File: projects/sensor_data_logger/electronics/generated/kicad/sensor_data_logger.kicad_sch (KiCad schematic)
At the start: 12 parts, among them J1 USB-C POWER, J2 UART DEBUG, U1 ESP32-S3-WROOM-1, U2 ICM-42688-P, U3 3V3 Buck

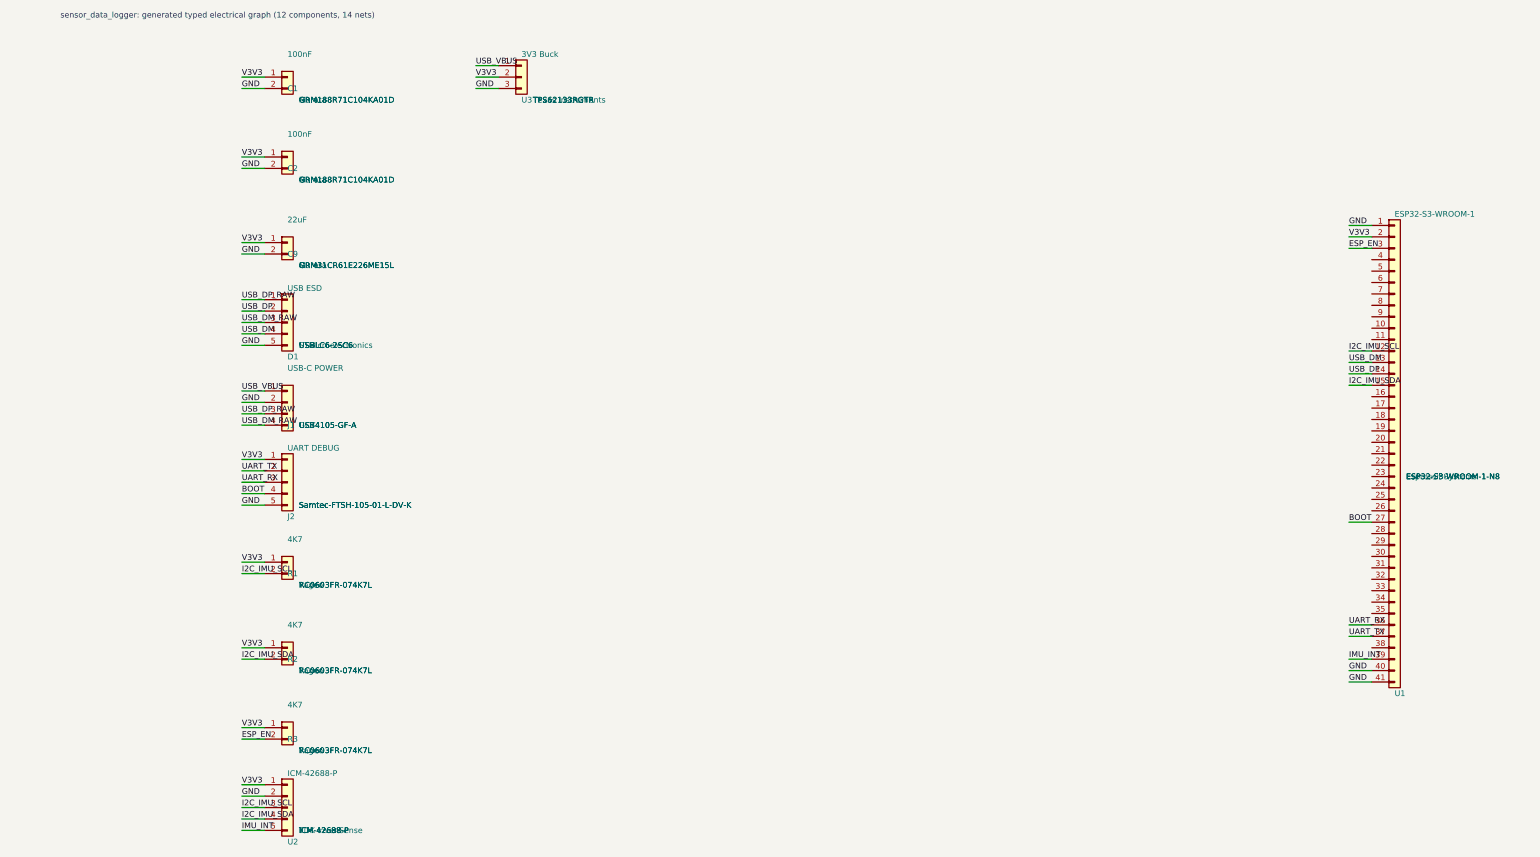
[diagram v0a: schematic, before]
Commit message: fix: sensor_data_logger autorouting pass; add BLE supplier records
- sensor_data_logger: freerouting run to completion, 0 unrouted (routing.json status=pass)
- parts/suppliers/curated.yaml: add nRF52840, BQ24079, BQ27441, JST PH 2-pin,
  SHT31 records for BLE sensor node to resolve supplier_record_missing failures
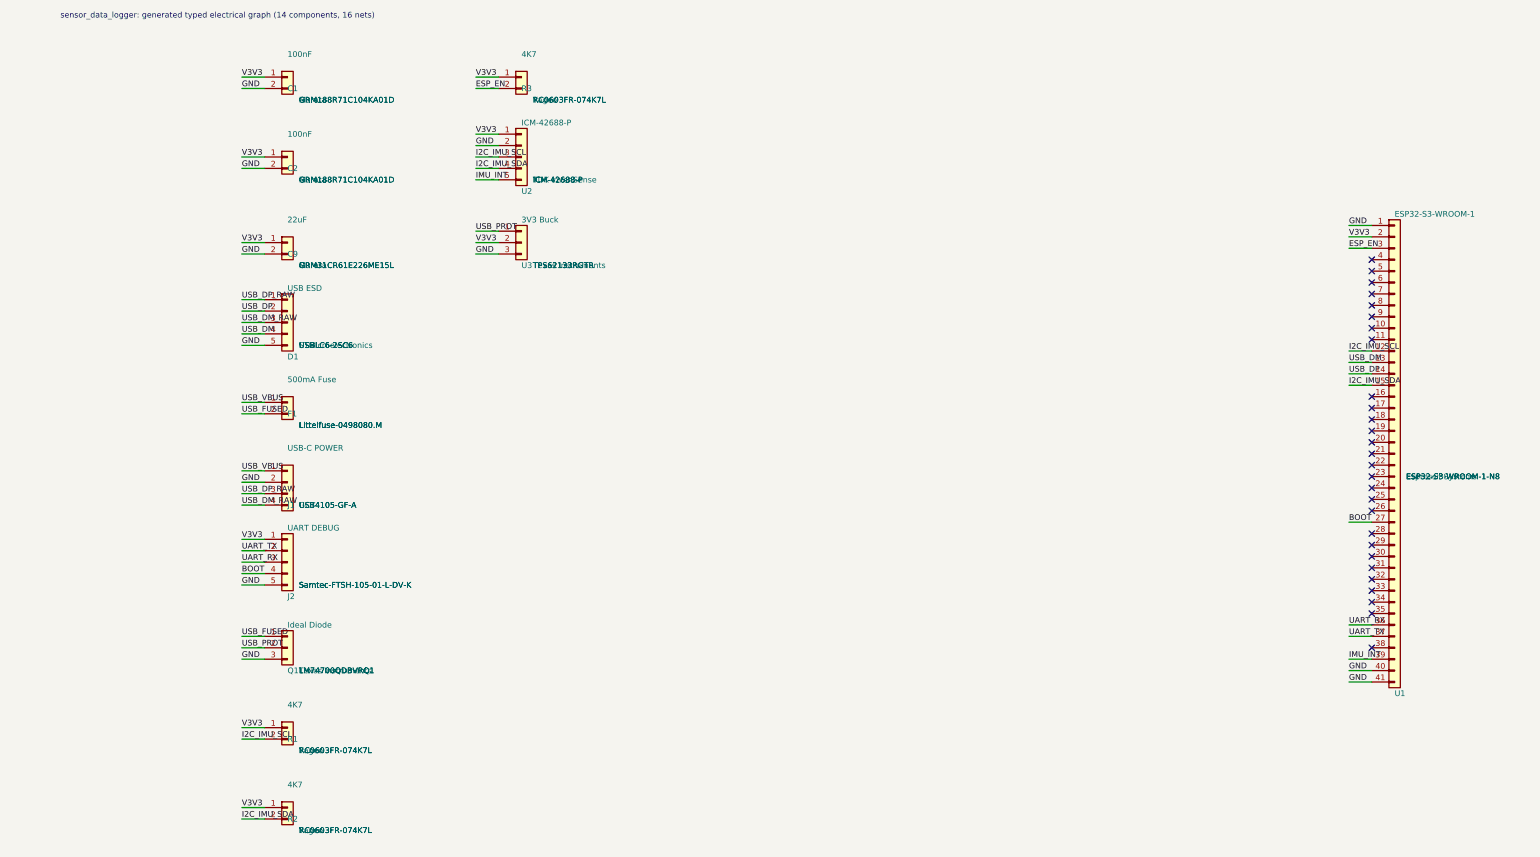
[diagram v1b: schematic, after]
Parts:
- added J1: USB-C POWER, USB_C_16Pin, symbol Connector_Generic:Conn_01x04
- added R2: 4K7, R0603, symbol Connector_Generic:Conn_01x02
- C1, C2: footprint Capacitor_SMD:C_0603_1608Metric -> C0603
- C9: footprint Capacitor_SMD:C_1206_3216Metric -> C1206
- D1: footprint Package_TO_SOT_SMD:SOT-23-6 -> SOT23-6
- F1: renamed from J1; value USB-C POWER -> 500mA Fuse; footprint Connector_USB:USB_C_GCT_USB4105 -> MIDI; symbol Connector_Generic:Conn_01x04 -> Connector_Generic:Conn_01x02; MPN USB4105-GF-A -> Littelfuse-0498080.M; Manufacturer GCT -> Littelfuse; Supplier_SKU USB4105-GF-A -> Littelfuse-0498080.M
- J2: footprint Connector_Samtec:FTSH-105 -> Cortex_Debug_10Pin
- Q1: renamed from R2; value 4K7 -> Ideal Diode; footprint Resistor_SMD:R_0603_1608Metric -> SOT23-6; symbol Connector_Generic:Conn_01x02 -> Connector_Generic:Conn_01x03; MPN RC0603FR-074K7L -> LM74700QDBVRQ1; Manufacturer Yageo -> Texas Instruments; Supplier_SKU RC0603FR-074K7L -> LM74700QDBVRQ1
- R1, R3: footprint Resistor_SMD:R_0603_1608Metric -> R0603
- U2: footprint Package_LGA:LGA-14 -> LGA14
- U3: footprint Package_DFN_QFN:VQFN-16 -> VQFN16
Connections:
- net GND: now also Q1.3 (Pin_3), J1.2 (Pin_2); no longer F1.2 (Pin_2)
- net I2C_IMU_SDA: now also R2.2 (Pin_2); no longer Q1.2 (Pin_2)
- net USB_DM_RAW: now also J1.4 (Pin_4); no longer F1.4 (Pin_4)
- net USB_DP_RAW: now also J1.3 (Pin_3); no longer F1.3 (Pin_3)
- net USB_VBUS: now also J1.1 (Pin_1); no longer U3.1 (Pin_1)
- net V3V3: now also R2.1 (Pin_1); no longer Q1.1 (Pin_1)
- new net USB_FUSED: F1.2 (Pin_2), Q1.1 (Pin_1)
- new net USB_PROT: Q1.2 (Pin_2), U3.1 (Pin_1)
- no-connect marks 0 -> 28
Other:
- note added: "sensor_data_logger: generated typed electrical graph (14 components, 16 nets)"
- note removed: "sensor_data_logger: generated typed electrical graph (12 components, 14 nets)"
